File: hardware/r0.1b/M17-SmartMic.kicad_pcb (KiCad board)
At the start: 4 copper layers, 84.9 x 89.9 mm, 166 parts, among them IC1 LM4861MX, J1 Kenwood-2.5, J10 UART, J2 USB_C, J3 OLED, J4 CAT_TX, J5 Kenwood-3.5, J6 CAT_RX, J7 Radio, J8 +12V, J9 STLink, Q1 IRLML2060, SW1 Button Up, SW2 Button Down, SW3 Reset, SW4 Button Escape, SW5 Button Left, SW6 Button Enter, SW7 Button Right, U1 MAX9814, U10 STM32F405RGTx, U11 TPS5431DDA, U2 LM1117-3.3, U3 USBLC6-2, U5 MAX3232, U6 MCP602, U7 MCP602, U8 MCP4551-103, U9 MCP4551-104, X1 12 MHz TCXO, Y1 8 MHz

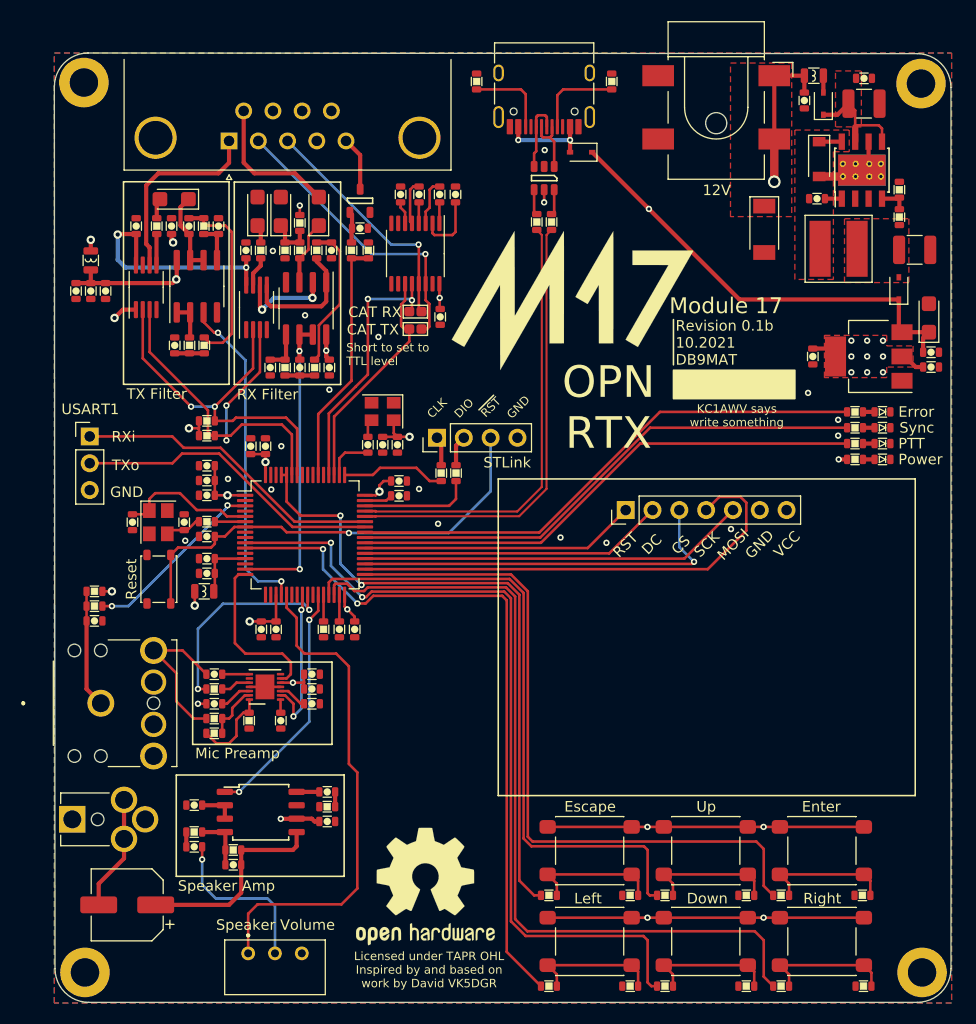
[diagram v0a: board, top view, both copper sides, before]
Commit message: Added RTC
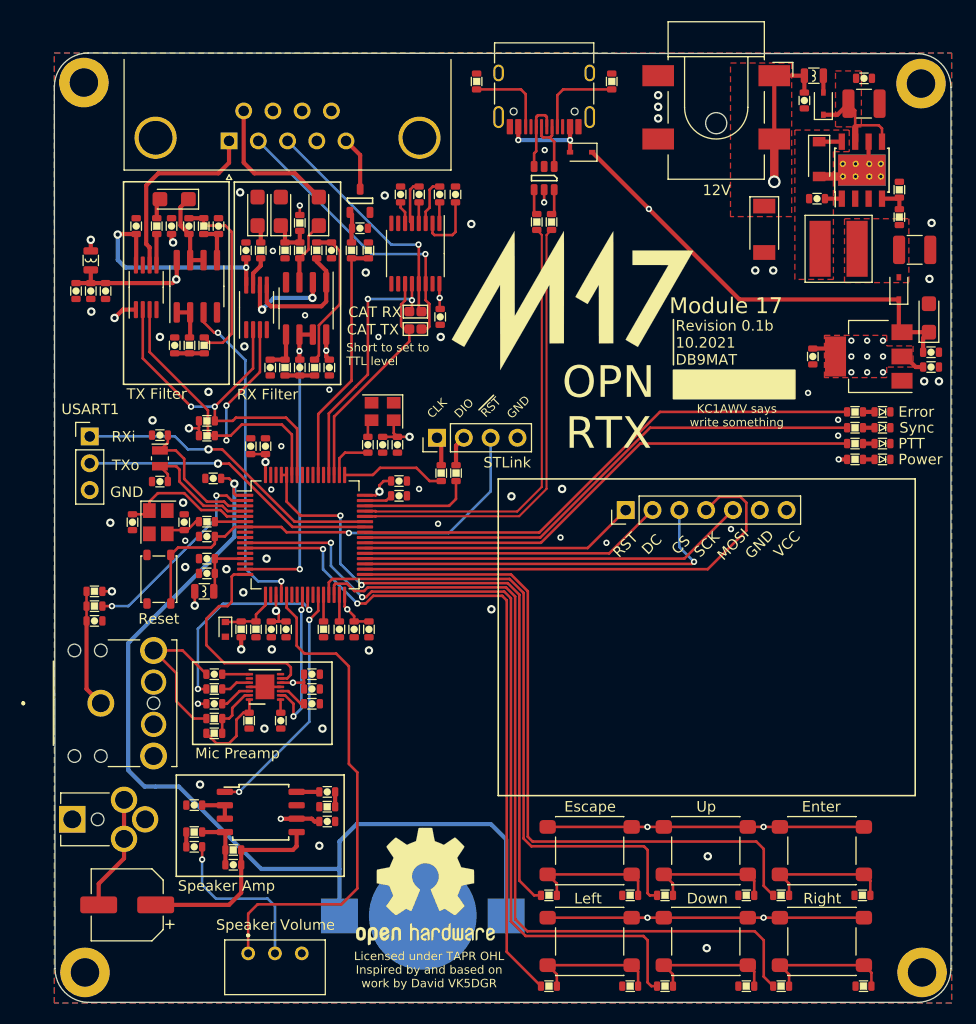
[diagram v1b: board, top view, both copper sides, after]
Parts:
- removed C10: 10n, pkl_dipol:C_0603
- removed C15: 100n, pkl_dipol:C_0603
- added BT1: Coin, Battery:BatteryHolder_Keystone_3000_1x12mm, B.Cu at (104.0, 115.8)
- added C66: 12p, pkl_dipol:C_0603, F.Cu at (79.1, 70.2)
- added C67: 12p, pkl_dipol:C_0603, F.Cu at (79.1, 74.6)
- added C68: 100n, pkl_dipol:C_0603, F.Cu at (84.2, 74.3)
- added D10: 3v3, Diode_SMD:D_SOD-523, F.Cu at (85.3, 88.6)
- added R53: 39k, pkl_dipol:R_0603, F.Cu at (86.8, 88.6)
- added R54: 10k, pkl_dipol:R_0603, F.Cu at (88.2, 88.6)
- added Y2: 32 kHz, Crystal:Crystal_SMD_MicroCrystal_CC8V-T1A-2Pin_2.0x1.2mm, F.Cu at (79.1, 72.4)
- moved C17 20.9 mm to (97.5, 88.6), turned to -90 degrees
- moved C16 20.8 mm to (98.9, 88.6), turned to -90 degrees
- moved C1 0.95 mm to (89.7, 88.6)
- moved C4 0.95 mm to (91.0, 88.6)
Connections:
- U10 pad 1: VDD -> VBAT
- U10 pad 17: unconnected-(U10-Pad17) -> Net-(U10-Pad17)
- U10 pad 2: unconnected-(U10-Pad2) -> ~{PTT_IN}
- U10 pad 3: ~{PTT_IN} -> Net-(U10-Pad3)
- U10 pad 4: unconnected-(U10-Pad4) -> Net-(U10-Pad4)
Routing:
- net +12V: track 59.9 -> 177.3 mm, vias 1 -> 2
- net VBAT: track 0.00 -> 90.1 mm, vias 0 -> 1
- net VAA: track 53.4 -> 104.7 mm
- net +5V: track 153.6 -> 177.3 mm
- net Net-(U10-Pad3): track 0.00 -> 13.1 mm
- net Net-(U10-Pad4): track 0.00 -> 12.3 mm
- net Net-(U10-Pad17): track 0.00 -> 5.82 mm
- net VDD: track 122.8 -> 117.5 mm, vias 28 -> 27
- net AUDIO_MIC: track 15.6 -> 20.0 mm
- net ~{PTT_IN}: track 17.6 -> 19.3 mm
- net USART1_TX: track 29.3 -> 28.6 mm, vias 0 -> 1
- net USART1_RX: vias 0 -> 1
- net GND: vias 18 -> 53
- removed copper zone on In1.Cu, net VAA

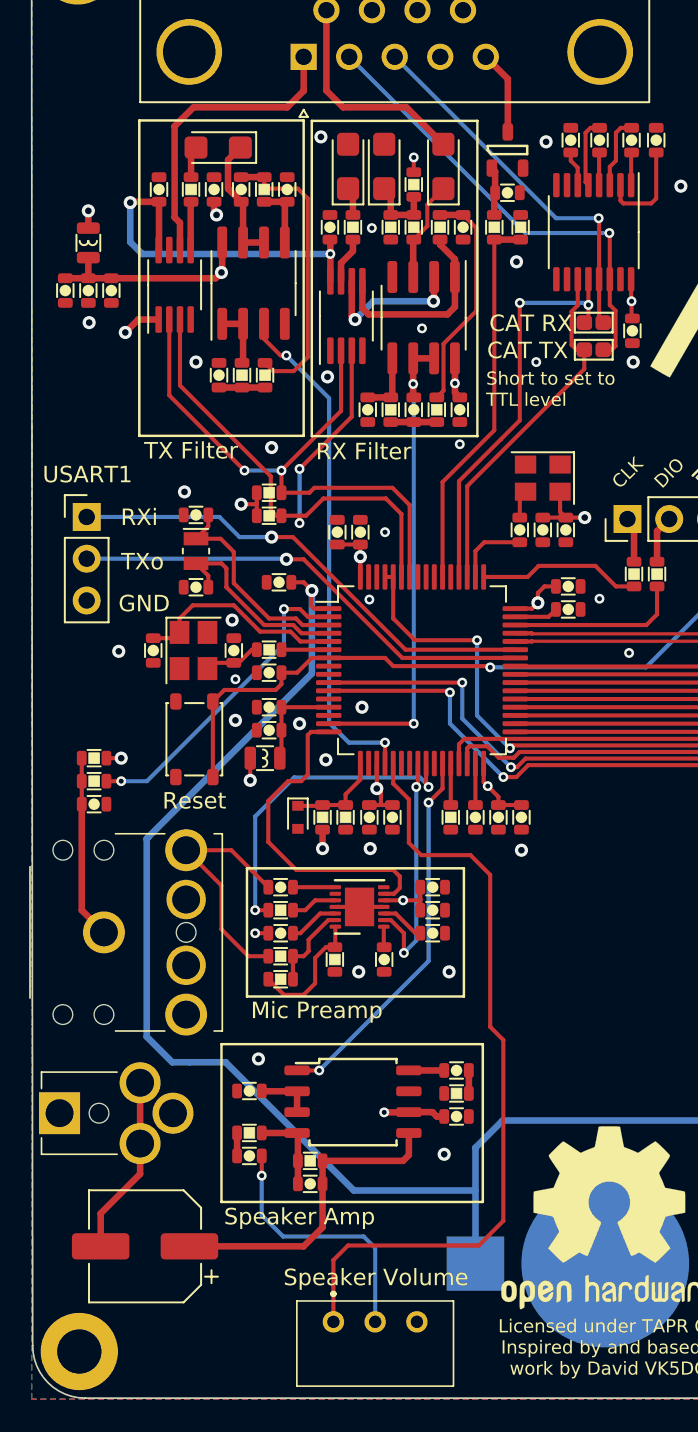
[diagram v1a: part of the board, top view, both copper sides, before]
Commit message: Added RTC and Test Points to r0.1b
This marks production for revision 0.1b
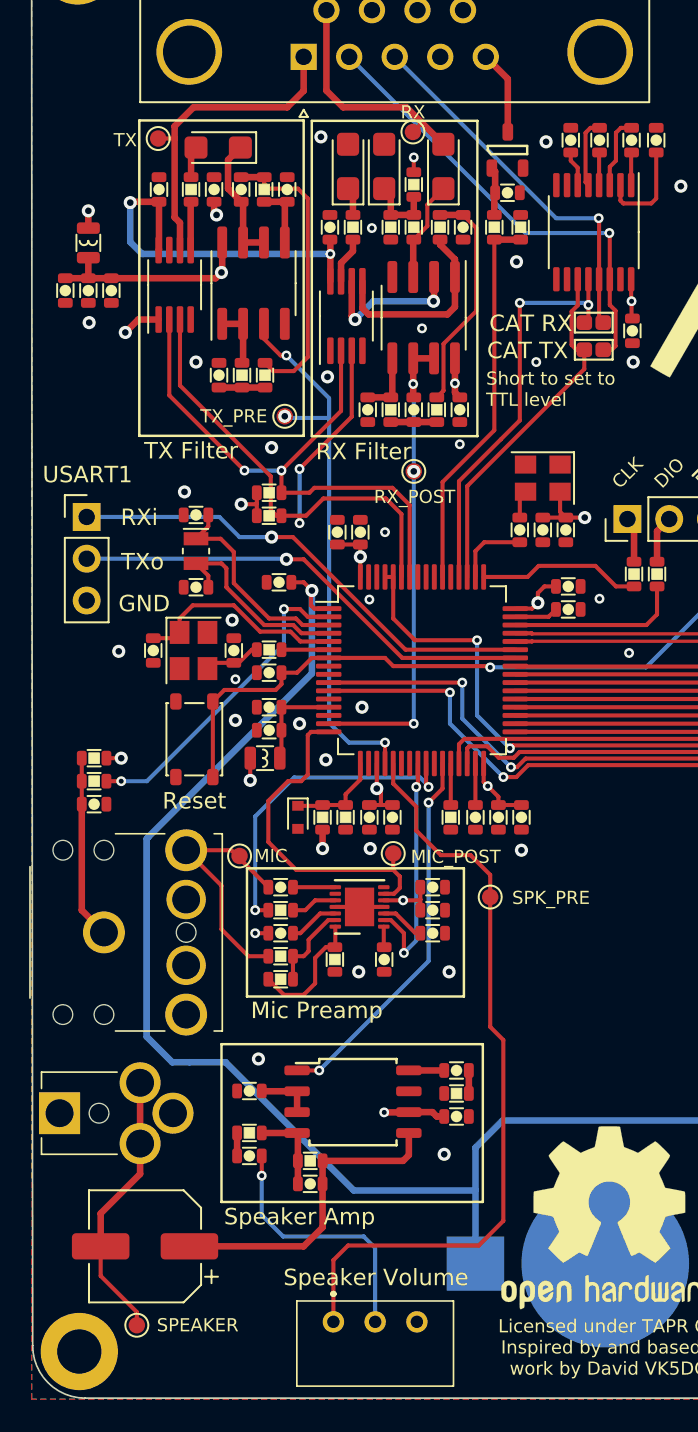
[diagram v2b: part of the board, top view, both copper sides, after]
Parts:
- added TP1: TP_MIC, TestPoint:TestPoint_Pad_D1.0mm, F.Cu at (81.8, 91.0)
- added TP2: TP_SPK_PRE, TestPoint:TestPoint_Pad_D1.0mm, F.Cu at (97.0, 93.5)
- added TP3: TP_MIC_POST, TestPoint:TestPoint_Pad_D1.0mm, F.Cu at (91.1, 90.8)
- added TP4: TP_SPK, TestPoint:TestPoint_Pad_D1.0mm, F.Cu at (75.5, 119.5)
- added TP5: TP_BBTX, TestPoint:TestPoint_Pad_D1.0mm, F.Cu at (84.5, 64.2)
- added TP6: TP_BBRX, TestPoint:TestPoint_Pad_D1.0mm, F.Cu at (92.3, 67.5)
- added TP7: TP_RX, TestPoint:TestPoint_Pad_D1.0mm, F.Cu at (92.3, 46.9)
- added TP8: TP_TX, TestPoint:TestPoint_Pad_D1.0mm, F.Cu at (76.8, 47.3)
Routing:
- net SPEAKER: track 10.9 -> 16.7 mm
- net BASEBAND_TX: track 31.3 -> 34.0 mm, vias 2 -> 3
- net RADIO_TX: track 18.5 -> 19.5 mm
- net AUDIO_MIC: track 20.0 -> 21.0 mm
- net RADIO_RX: track 13.4 -> 14.1 mm
- net AUDIO_SPK: track 47.4 -> 46.7 mm
- net BASEBAND_RX: vias 2 -> 3
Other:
- board text added: "MIC"
- board text added: "MIC_POST"
- board text added: "RX_POST"
- board text added: "SPEAKER"
- board text added: "SPK_PRE"
- board text added: "TX_PRE"
